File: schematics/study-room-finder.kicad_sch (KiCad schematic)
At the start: 0 parts

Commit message: add microphone and client MCU to schematic
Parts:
- added A1: Adafruit_Feather_HUZZAH_ESP8266, Module:Adafruit_Feather, symbol MCU_Module:Adafruit_Feather_HUZZAH_ESP8266
- added U1: ~, symbol mudasir_custom:Adafruit_Silicon_MEMS_Mic_Breakout
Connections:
- new net: A1.24 (IO12/MISO), U1. (VIN)
- new net +3.3V: A1.2 (3V3), U1. (VIN)
- new net GND: A1.4 (GND), U1. (VIN)
- no-connect marks 0 -> 8

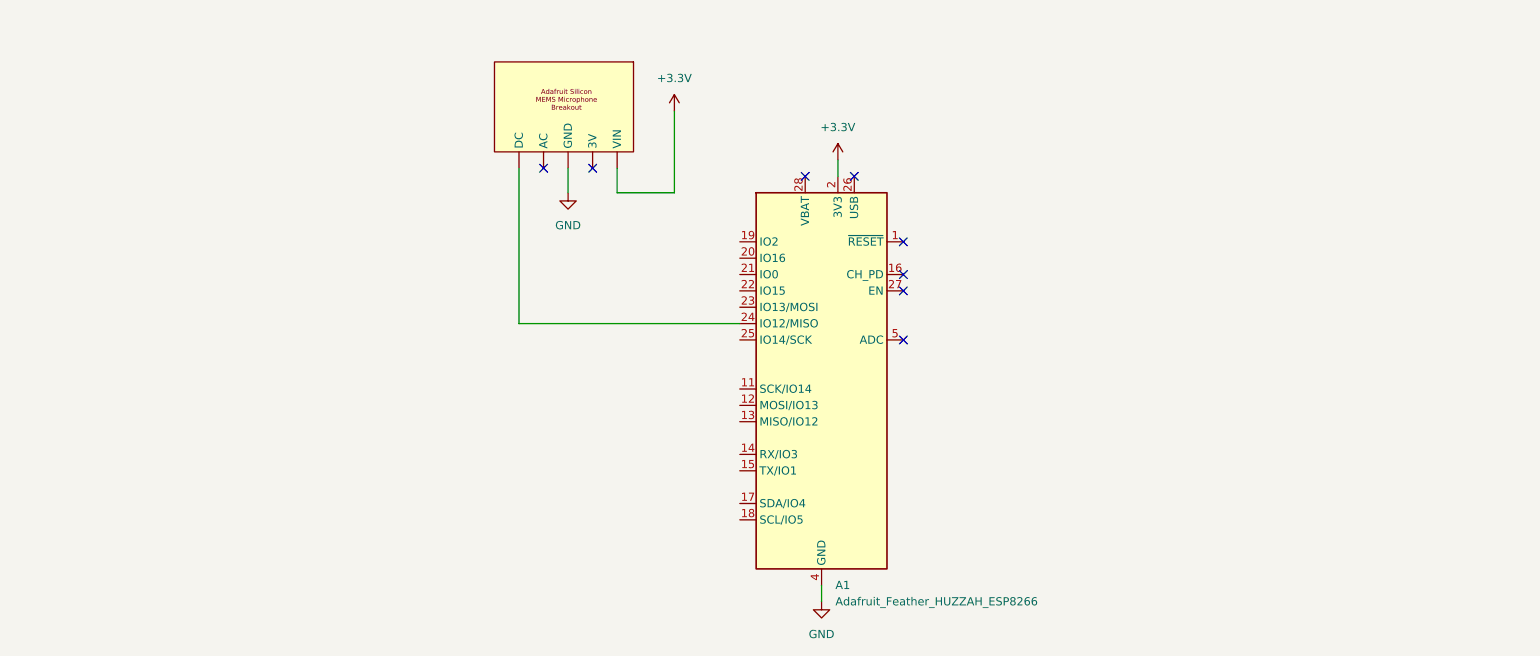
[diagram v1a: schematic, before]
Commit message: update MCU and add ultrasonic sensors to schematic
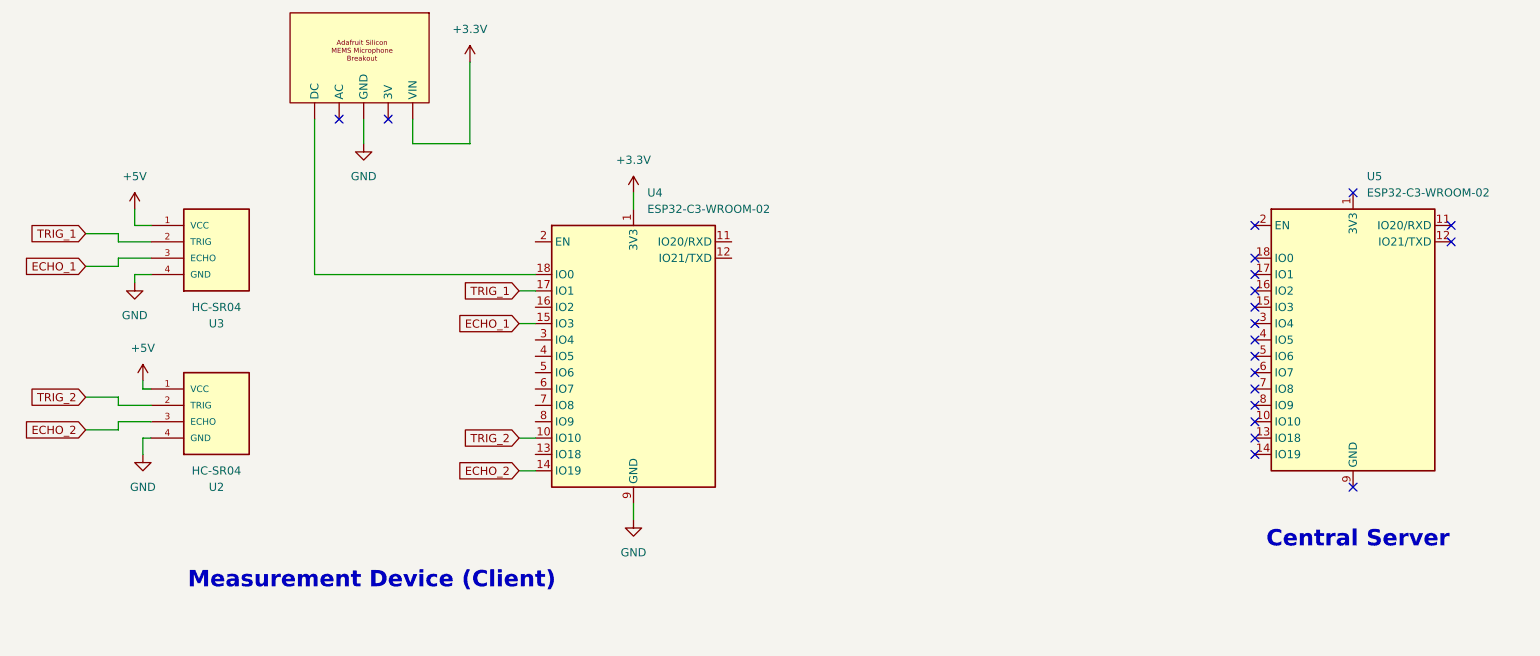
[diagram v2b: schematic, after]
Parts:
- removed A1: Adafruit_Feather_HUZZAH_ESP8266, Module:Adafruit_Feather, symbol MCU_Module:Adafruit_Feather_HUZZAH_ESP8266
- added U2, U3: HC-SR04, HC-SR04:XCVR_HC-SR04, symbol HC-SR04:HC-SR04
- added U4, U5: ESP32-C3-WROOM-02, RF_Module:ESP32-C3-WROOM-02, symbol RF_Module:ESP32-C3-WROOM-02
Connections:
- net +3.3V: now also U4.1 (3V3)
- net GND: now also U2.4 (GND), U3.4 (GND), U4.19 (GND), U4.9 (GND)
- new net: U5.19 (GND), U5.9 (GND)
- new net: U1. (VIN), U4.18 (IO0)
- new net +5V: U2.1 (VCC), U3.1 (VCC)
- new net ECHO_1: U3.3 (ECHO), U4.15 (IO3)
- new net ECHO_2: U2.3 (ECHO), U4.14 (IO19)
- new net TRIG_1: U3.2 (TRIG), U4.17 (IO1)
- new net TRIG_2: U2.2 (TRIG), U4.10 (IO10)
- no-connect marks 8 -> 20
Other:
- note added: "Central Server"
- note added: "Measurement Device (Client)"
